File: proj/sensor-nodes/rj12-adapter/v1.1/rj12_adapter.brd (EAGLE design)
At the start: 116.8 x 54.6 mm, 52 parts, among them J1 54602-908LF, J2 54602-908LF, J5 OPENAG-I2C-RJ12, J6 OPENAG-I2C-RJ12, U2 PCA9615, U3 MIC4680, U4 LM2937

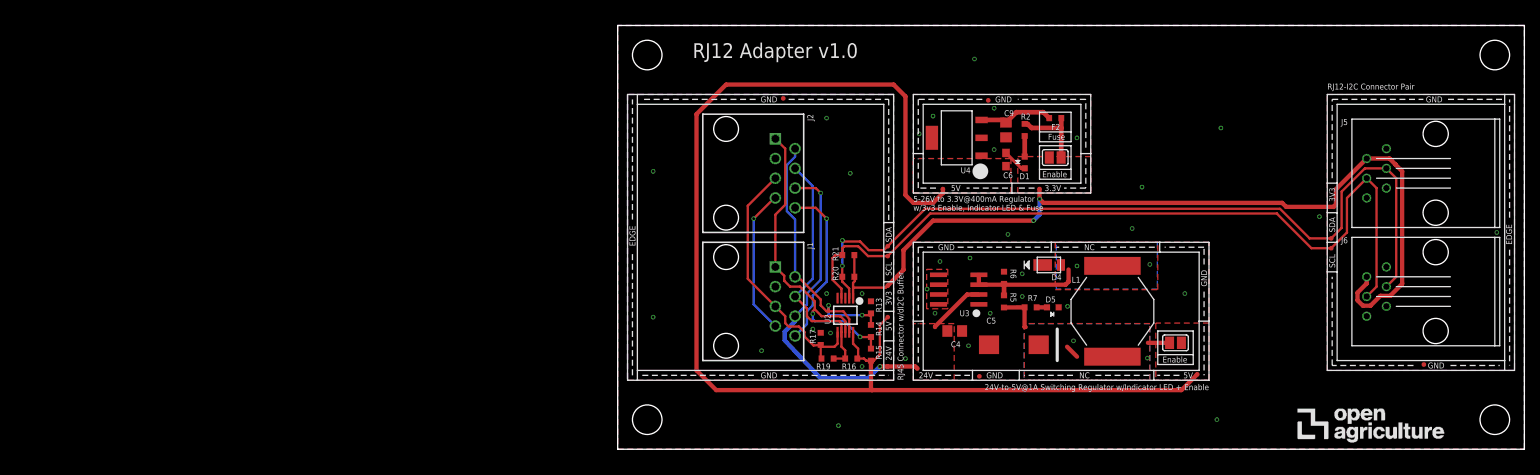
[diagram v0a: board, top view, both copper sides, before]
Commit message: added rj12 adapter v1.1
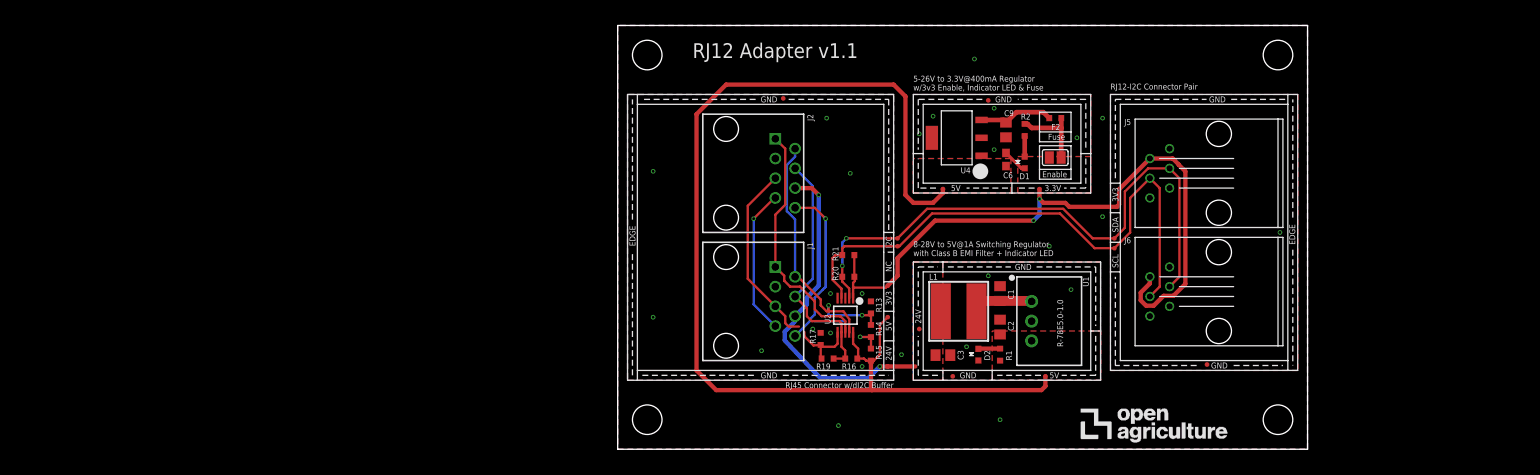
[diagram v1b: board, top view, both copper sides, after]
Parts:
- removed C4: 15uF, openag-capacitors:C0805
- removed C5: 220uF, openag-capacitors:CT7343
- removed D4: SBR2A40P1-7, openag-diodes:POWERDI123
- removed D5: APT1608, openag-diodes:CHIPLED_0603
- removed R5: 3.01K, openag-resistors:RC0603N
- removed R6: 976 Ohm, openag-resistors:RC0603N
- removed R7: 100, openag-resistors:RC0603N
- removed SJ2: (no value), openag-connectors:SOLDERJUMPER_REFLOW_NOPASTE
- removed TP5, TP6, TP7: TPTP06R, openag-testpads:TP06R
- removed U3: MIC4680, openag-regulators:SOIC8
- added C1, C2, C3: 10uF, openag-capacitors:C0805
- added D2: APT1608, openag-diodes:CHIPLED_0603
- added R1: 100, openag-resistors:RC0603N
- added TP1, TP2, TP3: TPTP06R, openag-testpads:TP06R
- added U1: R-78E5.0-1.0, openag-regulators:R-78E5.0-1.0
- L1: value 68uH -> 33uH; device openag-inductors:UP2B -> openag-inductors:29333C
- moved J5 27.9 mm to (77.5, 35.6)
- moved J6 27.9 mm to (77.5, 20.3)
- moved TP11 27.9 mm to (64.3, 31.2)
- moved TP12 27.9 mm to (64.0, 25.9)
- moved TP13 27.9 mm to (75.9, 10.9)
- moved TP14 27.9 mm to (64.0, 27.2)
- moved U$3 27.9 mm to (85.1, 3.81)
- moved U$4 27.9 mm to (85.1, 50.8)
- moved U$5 27.9 mm to (59.7, 1.27)
- moved FRAME1 24.4 mm to (65.8, 24.9)
- moved L1 19.8 mm to (43.9, 17.8), turned to 0 degrees
- moved TP8 1.80 mm to (36.1, 26.2)
- moved TP9 1.63 mm to (36.1, 27.2)
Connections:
- removed net N$31: D4.+, L1.1, R5.1, R6.2, U3.3, U3.4
- removed net N$32: D5.A, R7.1
- removed net N$33: C5.+, L1.2, R5.2, R7.2, SJ2.1
- new net 24V_EMI: C1.1, L1.P$2, U1.1
- new net N$6: D2.A, R1.1
- net +24V: now also C3.1, L1.P$1, TP1.TP; no longer C4.1, TP7.TP, U3.2
- net +5V: now also C2.1, R1.2, TP3.TP, U1.3; no longer SJ2.2, TP5.TP
- net GND: now also C1.2, C2.2, C3.2, D2.C, TP2.TP, U1.2; no longer C4.2, C5.-, D4.-, D5.C, R6.1, TP6.TP, U3.1, U3.5, U3.6, U3.7, U3.8
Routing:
- net SDA: track 105.0 -> 75.9 mm
- net SCL: track 102.9 -> 73.9 mm
- net +3V3: track 115.2 -> 87.1 mm
- net +5V: track 163.7 -> 144.8 mm
- net N$31: track 16.2 -> 0.00 mm, vias 2 -> 0
- net N$33: track 9.96 -> 0.00 mm, vias 2 -> 0
- net +24V: track 51.8 -> 43.5 mm
- net 24V_EMI: track 0.00 -> 7.68 mm
- net DSDAP: track 43.2 -> 38.6 mm, vias 2 -> 1
- net N$6: track 0.00 -> 2.81 mm
- net N$32: track 1.33 -> 0.00 mm
- net DSCLM: track 33.9 -> 32.9 mm
- net GND: vias 35 -> 26
- removed copper zone on layer 1, net N$31
- removed copper zone on layer 16, net N$31
- removed copper zone on layer 1, net N$33
- removed copper zone on layer 16, net N$33
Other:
- board size 116.8 x 54.6 mm -> 88.9 x 54.6 mm
- board text added: "8-28V to 5V@1A Switching Regulator with Class B EMI Filter + Indicator LED"
- board text added: "I2C"
- board text added: "RJ12 Adapter v1.1"
- board text removed: "24V-to-5V@1A Switching Regulator w/Indicator LED + Enable"
- board text removed: "RJ12 Adapter v1.0"

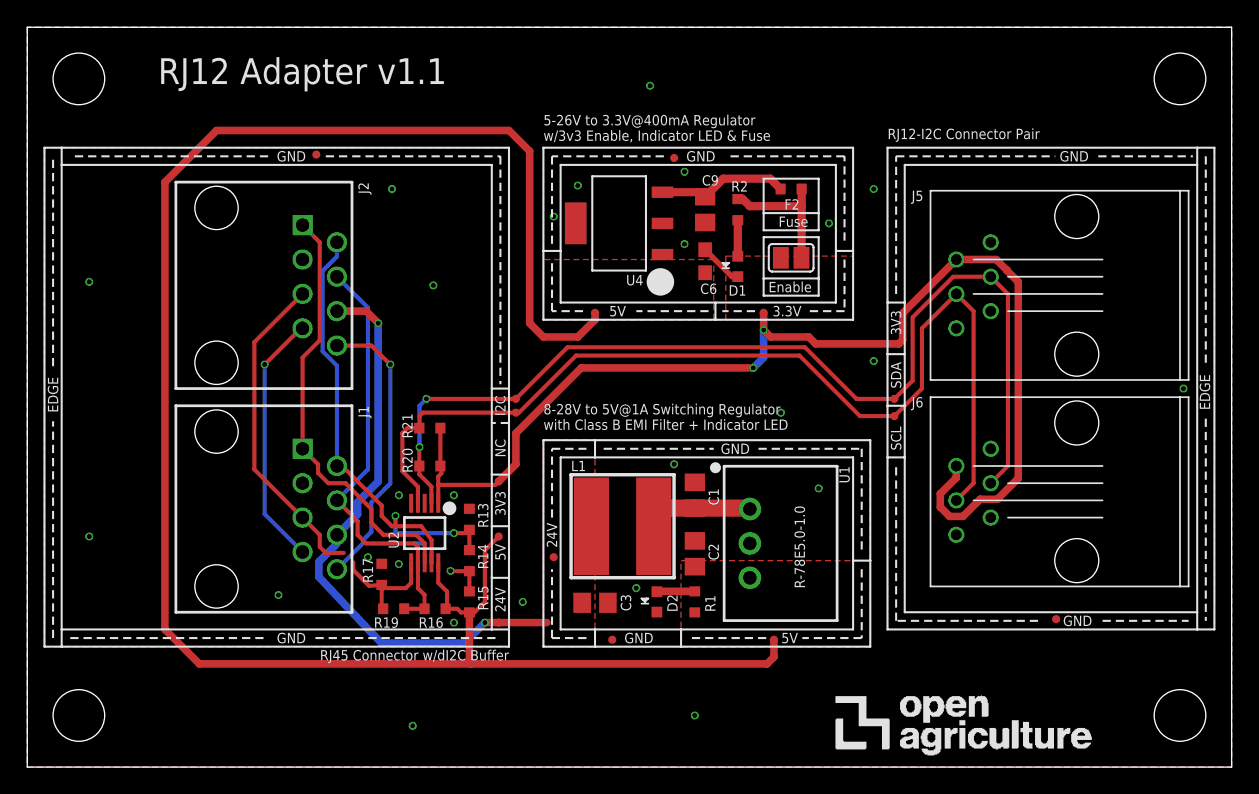
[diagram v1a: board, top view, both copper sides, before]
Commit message: cleaned up regulator design blocks
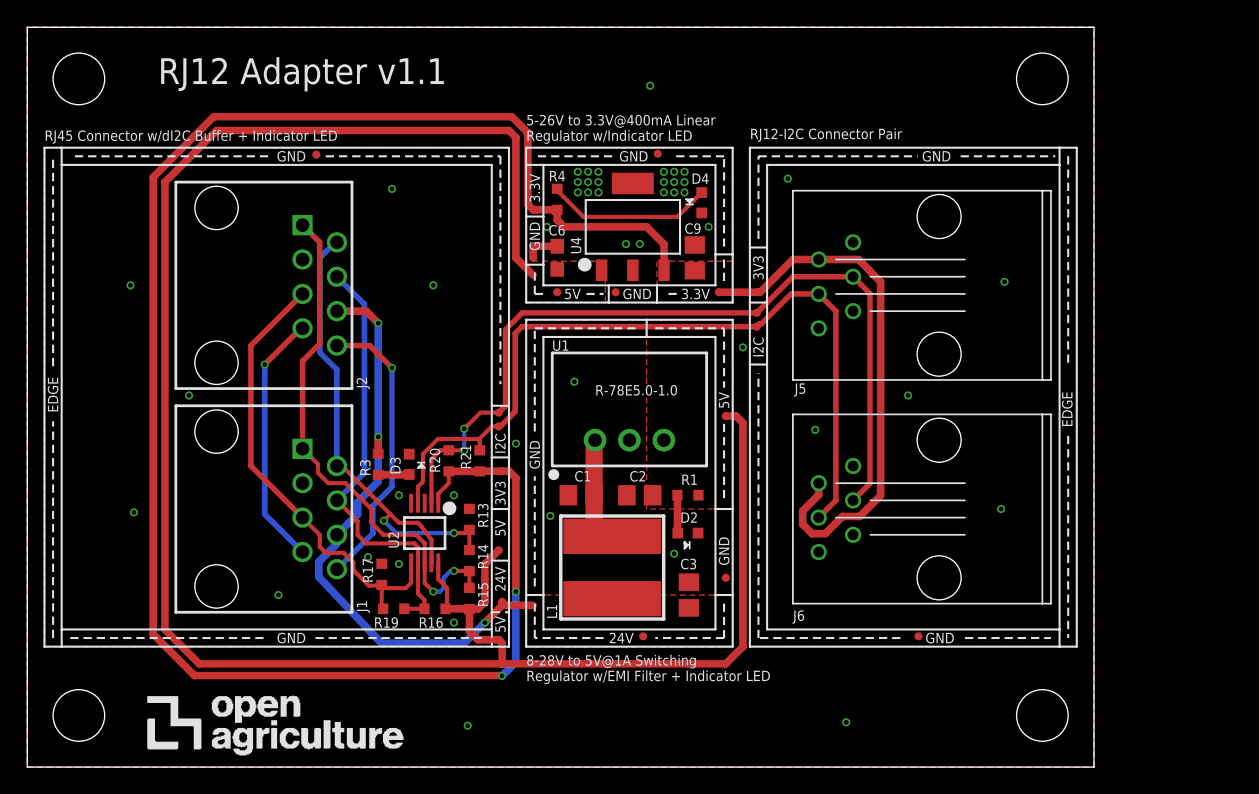
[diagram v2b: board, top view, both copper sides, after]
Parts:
- removed D1: APT1608, openag-diodes:CHIPLED_0603
- removed F2: 400mA, openag-fuses:0603
- removed R2: 100, openag-resistors:RC0603N
- removed SJ3: (no value), openag-connectors:SOLDERJUMPER_REFLOW_NOPASTE
- removed TP30: TPTP06R, openag-testpads:TP06R
- added D3, D4: APT1608, openag-diodes:CHIPLED_0603
- added R3, R4: 100, openag-resistors:RC0603N
- added TP10, TP15, TP5, TP6, TP7: TPTP06R, openag-testpads:TP06R
- moved U$5 50.8 mm to (8.89, 1.27)
- moved TP3 16.9 mm to (51.6, 25.9), turned to 270 degrees
- moved TP12 12.1 mm to (53.8, 32.5)
- moved TP14 12.0 mm to (53.8, 33.5)
- moved U1 11.7 mm to (44.5, 24.1), turned to 0 degrees
- moved TP11 11.1 mm to (53.9, 35.1)
- moved C6 10.9 mm to (39.1, 37.6)
- moved TP4 10.8 mm to (43.4, 35.1), turned to 0 degrees
- moved FRAME1 10.2 mm to (55.6, 23.6)
- moved J6 10.2 mm to (67.3, 19.1)
- moved TP13 10.2 mm to (65.8, 9.65)
- moved J5 10.2 mm to (67.3, 35.6)
- moved U$3 10.2 mm to (74.9, 3.81)
- moved U$4 10.2 mm to (74.9, 50.8)
- moved TP2 9.55 mm to (51.6, 14.0), turned to 270 degrees
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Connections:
- removed net N$4: D1.A, R2.1
- removed net REG_3V3_400MA: F2.2, R2.2, SJ3.1
- new net N$7: D3.A, R3.1
- net +24V: now also R3.2
- net +3V3: now also C9.1, R4.2, TP10.TP, TP7.TP, U4.3; no longer SJ3.2, TP30.TP
- net +5V: now also TP5.TP
- net GND: now also D3.C, D4.C, TP15.TP, TP6.TP; no longer D1.C
- net N$5: now also D4.A, R4.1; no longer C9.1, F2.1, U4.3
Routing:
- net +3V3: track 87.1 -> 172.7 mm
- net SCL: track 73.9 -> 59.7 mm
- net SDA: track 75.9 -> 62.0 mm
- net REG_3V3_400MA: track 10.0 -> 0.00 mm
- net +5V: track 144.8 -> 150.7 mm
- net N$4: track 2.66 -> 0.00 mm
- net N$7: track 0.00 -> 2.30 mm
- net N$5: track 10.1 -> 12.3 mm
- net DSCLM: track 32.9 -> 34.1 mm
- net +24V: track 43.5 -> 44.6 mm, vias 2 -> 3
- net DSDAP: track 38.6 -> 39.2 mm, vias 1 -> 2
- net GND: track 3.23 -> 2.63 mm, vias 26 -> 46
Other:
- board size 88.9 x 54.6 mm -> 78.7 x 54.6 mm
- board text added: "5-26V to 3.3V@400mA Linear Regulator w/Indicator LED"
- board text added: "8-28V to 5V@1A Switching Regulator w/EMI Filter + Indicator LED"
- board text added: "RJ45 Connector w/dI2C Buffer + Indicator LED"
- board text removed: "100"
- board text removed: "5-26V to 3.3V@400mA Regulator w/3v3 Enable, Indicator LED & Fuse"
- board text removed: "8-28V to 5V@1A Switching Regulator with Class B EMI Filter + Indicator LED"
- board text removed: "Enable"
- board text removed: "Fuse"
- board text removed: "NC"
- board text removed: "RJ45 Connector w/dI2C Buffer"
- board text removed: "SCL"
- board text removed: "SDA"

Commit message: improving keyboard shortcuts
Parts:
- removed J2: 54602-908LF, openag_connector:OPENAG-V1-RJ45
- added J3: 54602-908LF, openag_connector:OPENAG-V1-RJ45
- added R12, R22, R23, R24: 600, openag-resistors:RC0603N
- added R18, R25: 120, openag-resistors:RC0603N
- added U5: PCA9615, openag-buffers:SOP50P490X110-10N
- R3: value 100 -> 1K
- moved R13 78.8 mm to (-46.1, 17.0)
- moved R14 78.8 mm to (-46.1, 14.0)
- moved R15 78.8 mm to (-46.1, 11.2)
- moved R17 78.8 mm to (-52.6, 13.0)
- moved R21 78.8 mm to (-45.3, 21.3)
- moved R3 78.8 mm to (-52.8, 21.1)
- moved TP32 78.8 mm to (-43.7, 20.6)
- moved TP33 78.8 mm to (-57.4, 43.9)
- moved TP34 78.8 mm to (-43.9, 8.13)
- moved TP35 78.8 mm to (-43.7, 10.9)
- moved TP5 78.8 mm to (-43.9, 14.7)
- moved TP8 78.8 mm to (-43.9, 23.9)
- moved TP9 78.8 mm to (-43.9, 24.9)
- moved D3 78.8 mm to (-50.5, 21.1)
- moved J1 78.8 mm to (-64.8, 17.8)
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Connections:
- removed net DSCLM: J1.DSCLM(5), J2.DSCLM(5), R17.2, R19.1, U2.6
- removed net DSCLP: J1.DSCLP(4), J2.DSCLP(4), R16.1, R19.2, U2.7
- removed net DSDAM: J1.DSDAM(2), J2.DSDAM(2), R13.1, R14.2, U2.9
- removed net DSDAP: J1.DSDAP(1), J2.DSDAP(1), R14.1, R15.2, U2.8
- new net DSCLM_1: J1.DSCLM(5), R17.2, R19.1, U2.6
- new net DSCLM_2: J3.DSCLM(5), R24.2, R25.1, U5.6
- new net DSCLP_1: J1.DSCLP(4), R16.1, R19.2, U2.7
- new net DSCLP_2: J3.DSCLP(4), R23.1, R25.2, U5.7
- new net DSDAM_1: J1.DSDAM(2), R13.1, R14.2, U2.9
- new net DSDAM_2: J3.DSDAM(2), R12.1, R18.2, U5.9
- new net DSDAP_1: J1.DSDAP(1), R14.1, R15.2, U2.8
- new net DSDAP_3: J3.DSDAP(1), R18.1, R22.2, U5.8
- net +24V: now also J3.24V(6); no longer J2.24V(6)
- net +3V3: now also U5.1
- net +5V: now also R22.1, R23.2, U5.10
- net GND: now also J3.GND(3), R12.2, R24.1, U5.5; no longer J2.GND(3)
- net SCL: now also U5.4
- net SDA: now also U5.2
- net USBM: now also J3.USBM(8); no longer J2.USBM(8)
- net USBP: now also J3.USBP(7); no longer J2.USBP(7)
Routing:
- net +3V3: track 172.7 -> 100.2 mm, vias 2 -> 4
- net +5V: track 150.7 -> 81.6 mm
- net DSDAP: track 39.2 -> 0.00 mm, vias 2 -> 0
- net DSDAM: track 37.8 -> 0.00 mm, vias 2 -> 0
- net DSCLM: track 34.1 -> 0.00 mm
- net DSCLP: track 32.4 -> 0.00 mm
- net DSDAP_3: track 0.00 -> 21.7 mm, vias 0 -> 2
- net DSDAP_1: track 0.00 -> 21.7 mm, vias 0 -> 2
- net DSDAM_1: track 0.00 -> 19.8 mm, vias 0 -> 2
- net DSDAM_2: track 0.00 -> 19.7 mm, vias 0 -> 2
- net DSCLM_1: track 0.00 -> 14.4 mm
- net DSCLM_2: track 0.00 -> 14.4 mm
- net DSCLP_1: track 0.00 -> 14.3 mm
- net DSCLP_2: track 0.00 -> 13.7 mm
- net SCL: track 59.7 -> 73.0 mm, vias 0 -> 2
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
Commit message: cleaned up routing on di2c rj45 module
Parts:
- removed R12, R22, R23, R24: 600, openag-resistors:RC0603N
- removed R18, R25: 120, openag-resistors:RC0603N
- removed TP32, TP33, TP34, TP35: TPTP06R, openag-testpads:TP06R
- added R2, R5, R6, R7: 600, openag-resistors:RC0603N
- added R8, R9: 120, openag-resistors:RC0603N
- added TP16, TP17, TP18, TP19, TP20, TP21, TP22, TP23, TP24, TP25, TP26: TPTP04R, openag-testpads:TP04R
- TP5, TP8, TP9: value TPTP06R -> TPTP04R; device openag-testpads:TP06R -> openag-testpads:TP04R
- moved R3 148.3 mm to (95.5, 22.1)
- moved D3 146.2 mm to (95.5, 14.7)
- moved R19 79.5 mm to (27.7, 15.5)
- moved TP9 78.9 mm to (34.8, 20.3)
- moved TP8 78.8 mm to (34.8, 21.1)
- moved J1 78.8 mm to (14.0, 19.1)
- moved J3 78.8 mm to (14.0, 35.6)
- moved R17 78.0 mm to (25.4, 14.7), turned to 90 degrees
- moved R20 77.8 mm to (30.1, 24.9)
- moved R13 77.6 mm to (31.5, 18.5)
- moved R21 77.6 mm to (32.1, 24.9)
- moved U2 77.4 mm to (27.8, 20.6)
- moved U5 77.4 mm to (27.8, 37.1)
- moved R15 76.9 mm to (30.7, 14.0), turned to 180 degrees
- moved R14 76.9 mm to (30.7, 15.5), turned to 0 degrees
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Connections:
- net +24V: now also TP19.1, TP23.1; no longer TP35.TP
- net +3V3: now also TP21.1, TP5.1; no longer TP32.TP
- net +5V: now also R5.1, R7.2, TP16.1, TP22.1; no longer R22.1, R23.2, TP34.TP, TP5.TP
- net DSCLM_2: now also R6.2, R8.1; no longer R24.2, R25.1
- net DSCLP_2: now also R7.1, R8.2; no longer R23.1, R25.2
- net DSDAM_2: now also R2.1, R9.2; no longer R12.1, R18.2
- net DSDAP_3: now also R5.2, R9.1; no longer R18.1, R22.2
- net GND: now also R2.2, R6.1, TP17.1, TP24.1; no longer R12.2, R24.1, TP33.TP
- net SCL: now also TP25.1, TP9.1; no longer TP8.TP
- net SDA: now also TP26.1, TP8.1; no longer TP9.TP
- net USBM: now also TP20.1
- net USBP: now also TP18.1
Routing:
- net +5V: track 81.6 -> 171.6 mm, vias 0 -> 6
- net +3V3: track 100.2 -> 150.6 mm
- net SDA: track 68.2 -> 95.3 mm
- net SCL: track 73.0 -> 100.0 mm
- net +24V: track 40.5 -> 66.7 mm
- net USBM: track 19.4 -> 13.3 mm
- net DSDAM_1: track 19.8 -> 14.6 mm, vias 2 -> 0
- net DSDAM_2: track 19.7 -> 14.7 mm, vias 2 -> 0
- net DSDAP_1: track 21.7 -> 16.7 mm, vias 2 -> 0
- net DSDAP_3: track 21.7 -> 16.9 mm, vias 2 -> 0
- net DSCLP_1: track 14.3 -> 10.5 mm
- net DSCLM_1: track 14.4 -> 11.0 mm
- net DSCLP_2: track 13.7 -> 10.5 mm
- net DSCLM_2: track 14.4 -> 11.5 mm
- net N$7: track 2.30 -> 0.00 mm
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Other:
- board text added: "SCL"
